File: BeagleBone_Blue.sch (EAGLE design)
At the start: 409 parts, among them J1 68000-406HLF, M1 JST_ZH_2, M2 JST_ZH_2, M3 JST_ZH_2, M4 JST_ZH_2, P10 SCHA5B0200, P2 CTIJTAG, P3 87520-0010BLF, P4 UX60SC-MB-5ST(80), Q3 MOSFET-N, Q4 MOSFET-P, U1 MPU-9250, U10 TPD4S012, U12 MT41K256M16HA, U13 MTFC4GLDEA, U15 SN74LVC2G241DCU, U16 SN74LVC1G07DCK, U3 SN74LVC1G06DCK, U4 TL5209, U5 AM3358_BZCZ_324, U6 SN74LVC1G74_DCT_8, U7 24LC_32AT-I/OT, U8 TPS2051BD, U9 TPD4S012, Y1 CM200C-32.768KAZF-UT, Y2 445C33D24M00000, Y4 ASDMB-24.576MHZ-LC-T

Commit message: Updates based on review
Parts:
- removed 108: (no value), rcl:C-EUC0402
- added C$108: 10uF 25V, SparkFun-Capacitors:CAP0805
- C108: value 10uF 25V -> (none); device SparkFun-Capacitors:CAP0805 -> rcl:C-EUC0402
- R50, R51: value (none) -> DNP
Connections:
- removed net N$242: R50.1, U5G$2.ECAP0_IN_PWM0_OUT/UART3_TXD/SPI1_CS1/PR1_ECAP0_ECAP_CAPIN_APWM_O/SPI1_SCLK/MMC0_SDWP/XDMA_EVENT_INTR2/GPIO0_7
- removed net N$244: R51.1, U5G$2.MCASP0_ACLKR/EQEP0A_IN/MCASP0_AXR2/MCASP1_ACLKX/MMC0_SDWP/PR1_PRU0_PRU_R30_4/PR1_PRU0_PRU_R31_4/GPIO3_18
- removed net SPI1_CS1: SPI1.2.6, U5G$1.GPMC_A1/GMII2_RXDV/RGMII2_RCTL/MMC2_DAT0/GPMC_A17/PR1_MII1_TXD3/EHRPWM1_SYNCI_O/GPIO1_17
- new net GPIO0_7SRC: R50.1, SPI1.2.6, U5G$2.ECAP0_IN_PWM0_OUT/UART3_TXD/SPI1_CS1/PR1_ECAP0_ECAP_CAPIN_APWM_O/SPI1_SCLK/MMC0_SDWP/XDMA_EVENT_INTR2/GPIO0_7
- new net GPIO1_17: U5G$1.GPMC_A1/GMII2_RXDV/RGMII2_RCTL/MMC2_DAT0/GPMC_A17/PR1_MII1_TXD3/EHRPWM1_SYNCI_O/GPIO1_17
- new net P9_42: R50.2, R51.2
- net GND: now also C$108.2; no longer 108.2
- net N$79: now also C$108.1; no longer C108.1
- net QEP_0A: now also R51.1, U5G$2.MCASP0_ACLKR/EQEP0A_IN/MCASP0_AXR2/MCASP1_ACLKX/MMC0_SDWP/PR1_PRU0_PRU_R30_4/PR1_PRU0_PRU_R31_4/GPIO3_18; no longer R50.2, R51.2
- net VCC: now also C108.1; no longer 108.1
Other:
- note removed: "GPIO0_7SRC"
- note removed: "GPIO3_18"
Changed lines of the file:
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@@
 <part name="R49" library="rcl" deviceset="R-US_" device="R0402"/>
 <part name="SUPPLY41" library="supply2" deviceset="GND" device="" value="DGND"/>
-<part name="R50" library="rcl" deviceset="R-US_" device="R0402"/>
-<part name="R51" library="rcl" deviceset="R-US_" device="R0402"/>
+<part name="R50" library="rcl" deviceset="R-US_" device="R0402" value="DNP"/>
+<part name="R51" library="rcl" deviceset="R-US_" device="R0402" value="DNP"/>
 <part name="U8" library="TPS2051B" deviceset="TPS2051B_D_8" device="" value="TPS2051BD"/>
 <part name="R53" library="rcl" deviceset="R-US_" device="R0402"/>
@@
 <part name="SUPPLY118" library="supply2" deviceset="GND" device="" value="DGND"/>
 <part name="C107" library="rcl" deviceset="C-EU" device="C0402"/>
-<part name="108" library="rcl" deviceset="C-EU" device="C0402"/>
+<part name="C108" library="rcl" deviceset="C-EU" device="C0402"/>
 <part name="C109" library="rcl" deviceset="C-EU" device="C0402"/>
 <part name="C110" library="rcl" deviceset="C-EU" device="C0402"/>
@@
 <part name="R39" library="Strawson_Eagle_Lib" deviceset="RESISTOR" device="0402-RES" value="4.7k"/>
 <part name="GND17" library="SparkFun-Aesthetics" deviceset="GND" device=""/>
-<part name="C108" library="SparkFun-Capacitors" deviceset="CAP" device="0805" value="10uF 25V"/>
+<part name="C$108" library="SparkFun-Capacitors" deviceset="CAP" device="0805" value="10uF 25V"/>
 <part name="C174" library="SparkFun-Capacitors" deviceset="CAP" device="0805" value="10uF 25V"/>
 <part name="C175" library="SparkFun-Capacitors" deviceset="CAP" device="0805" value="10uF 25V"/>
@@
 </segment>
 </net>
-<net name="SPI1_CS1" class="0">
+<net name="GPIO1_17" class="0">
 <segment>
 <pinref part="U5" gate="G$1" pin="GPMC_A1/GMII2_RXDV/RGMII2_RCTL/MMC2_DAT0/GPMC_A17/PR1_MII1_TXD3/EHRPWM1_SYNCI_O/GPIO1_17"/>
@@
 <text x="154.94" y="228.6" size="1.778" layer="96">USB1_DRVVBUS</text>
 <text x="157.48" y="226.06" size="1.778" layer="96">USB1_VBUS</text>
-<text x="152.4" y="210.82" size="1.778" layer="96">GPIO0_7SRC</text>
-<text x="162.56" y="200.66" size="1.778" layer="96">GPIO3_18</text>
 <text x="22.86" y="101.6" size="1.778" layer="96">USB1_DRVVBUS</text>
 <text x="111.76" y="109.22" size="1.778" layer="96">USB1_PWR</text>
@@
 </segment>
 </net>
-<net name="N$242" class="0">
+<net name="GPIO0_7SRC" class="0">
 <segment>
 <pinref part="R50" gate="G$1" pin="1"/>
 <pinref part="U5" gate="G$2" pin="ECAP0_IN_PWM0_OUT/UART3_TXD/SPI1_CS1/PR1_ECAP0_ECAP_CAPIN_APWM_O/SPI1_SCLK/MMC0_SDWP/XDMA_EVENT_INTR2/GPIO0_7"/>
 <wire x1="142.24" y1="210.82" x2="172.72" y2="210.82" width="0.1524" layer="91"/>
+<label x="152.4" y="210.82" size="1.778" layer="95"/>
 </segment>
 </net>
-<net name="QEP_0A" class="0">
+<net name="P9_42" class="0">
 <segment>
 <pinref part="R50" gate="G$1" pin="2"/>
@@
 </segment>
 </net>
-<net name="N$244" class="0">
+<net name="QEP_0A" class="0">
 <segment>
 <pinref part="R51" gate="G$1" pin="1"/>
@@
 <pinref part="U5" gate="G$2" pin="MCASP0_ACLKR/EQEP0A_IN/MCASP0_AXR2/MCASP1_ACLKX/MMC0_SDWP/PR1_PRU0_PRU_R30_4/PR1_PRU0_PRU_R31_4/GPIO3_18"/>
 <wire x1="436.88" y1="220.98" x2="419.1" y2="220.98" width="0.1524" layer="91"/>
+<label x="167.64" y="200.66" size="1.778" layer="95"/>
+<label x="436.88" y="220.98" size="1.778" layer="95"/>
 </segment>
 </net>
@@
 <instance part="SUPPLY118" gate="GND" x="182.88" y="355.6" rot="R270"/>
 <instance part="C107" gate="G$1" x="358.14" y="231.14"/>
-<instance part="108" gate="G$1" x="365.76" y="231.14"/>
+<instance part="C108" gate="G$1" x="365.76" y="231.14"/>
 <instance part="C109" gate="G$1" x="373.38" y="231.14"/>
 <instance part="C110" gate="G$1" x="381" y="231.14"/>
@@
 <wire x1="426.72" y1="215.9" x2="434.34" y2="215.9" width="0.1524" layer="91"/>
 <wire x1="434.34" y1="215.9" x2="434.34" y2="226.06" width="0.1524" layer="91"/>
-<pinref part="108" gate="G$1" pin="2"/>
+<pinref part="C108" gate="G$1" pin="2"/>
 <wire x1="365.76" y1="226.06" x2="365.76" y2="215.9" width="0.1524" layer="91"/>
 <pinref part="C109" gate="G$1" pin="2"/>
@@
 <pinref part="C109" gate="G$1" pin="1"/>
 <wire x1="373.38" y1="233.68" x2="373.38" y2="241.3" width="0.1524" layer="91"/>
-<pinref part="108" gate="G$1" pin="1"/>
+<pinref part="C108" gate="G$1" pin="1"/>
 <wire x1="365.76" y1="233.68" x2="365.76" y2="241.3" width="0.1524" layer="91"/>
 <junction x="365.76" y="241.3"/>
@@
 <instance part="R39" gate="G$1" x="102.87" y="-99.06" rot="R270"/>
 <instance part="GND17" gate="1" x="102.87" y="-107.95"/>
-<instance part="C108" gate="G$1" x="129.54" y="-11.43" smashed="yes">
+<instance part="C$108" gate="G$1" x="129.54" y="-11.43" smashed="yes">
 <attribute name="NAME" x="131.064" y="-8.509" size="1.778" layer="95"/>
 <attribute name="VALUE" x="127.889" y="-17.526" size="1.778" layer="96" rot="R90"/>
@@
 <pinref part="D11" gate="G$1" pin="C"/>
 <pinref part="D10" gate="G$1" pin="C"/>
-<pinref part="C108" gate="G$1" pin="1"/>
+<pinref part="C$108" gate="G$1" pin="1"/>
 <wire x1="132.08" y1="-1.27" x2="129.54" y2="-1.27" width="0.1524" layer="91"/>
 <wire x1="129.54" y1="-1.27" x2="129.54" y2="1.27" width="0.1524" layer="91"/>
@@
 <pinref part="D9" gate="G$1" pin="A"/>
 <wire x1="161.29" y1="-12.7" x2="161.29" y2="-19.05" width="0.1524" layer="91"/>
-<pinref part="C108" gate="G$1" pin="2"/>
+<pinref part="C$108" gate="G$1" pin="2"/>
 <pinref part="C174" gate="G$1" pin="2"/>
 <wire x1="182.88" y1="-12.7" x2="182.88" y2="-19.05" width="0.1524" layer="91"/>
@@
 </segment>
 </net>
-<net name="SPI1_CS1" class="0">
-<segment>
-<wire x1="236.22" y1="-114.3" x2="222.25" y2="-114.3" width="0.1524" layer="91"/>
-<label x="223.52" y="-114.3" size="1.778" layer="95"/>
-<pinref part="SPI1.2" gate="G$1" pin="6"/>
-</segment>
-</net>
 <net name="IMU_INT" class="0">
 <segment>
@@
 </segment>
 </net>
-<net name="QEP_0A" class="0">
-<segment>
-<wire x1="231.14" y1="-54.61" x2="218.44" y2="-54.61" width="0.1524" layer="91"/>
-<label x="232.41" y="-54.61" size="1.778" layer="95" rot="MR0"/>
-<pinref part="R168" gate="G$1" pin="1"/>
-<wire x1="218.44" y1="-50.8" x2="218.44" y2="-54.61" width="0.1524" layer="91"/>
-<pinref part="E1" gate="G$1" pin="3"/>
-</segment>
-</net>
 <net name="UART2_TX" class="0">
 <segment>
@@
 </segment>
 </net>
+<net name="GPIO0_7SRC" class="0">
+<segment>
+<pinref part="SPI1.2" gate="G$1" pin="6"/>
+<wire x1="236.22" y1="-114.3" x2="223.52" y2="-114.3" width="0.1524" layer="91"/>
+<label x="223.52" y="-114.3" size="1.778" layer="95"/>
+</segment>
+</net>
+<net name="QEP_0A" class="0">
+<segment>
+<pinref part="R168" gate="G$1" pin="1"/>
+<wire x1="218.44" y1="-50.8" x2="220.98" y2="-50.8" width="0.1524" layer="91"/>
+<wire x1="220.98" y1="-50.8" x2="220.98" y2="-54.61" width="0.1524" layer="91"/>
+<wire x1="220.98" y1="-54.61" x2="231.14" y2="-54.61" width="0.1524" layer="91"/>
+<wire x1="231.394" y1="-54.61" x2="231.14" y2="-54.61" width="0.1524" layer="91"/>
+<pinref part="E1" gate="G$1" pin="3"/>
+<label x="223.012" y="-54.102" size="1.778" layer="95"/>
+</segment>
+</net>

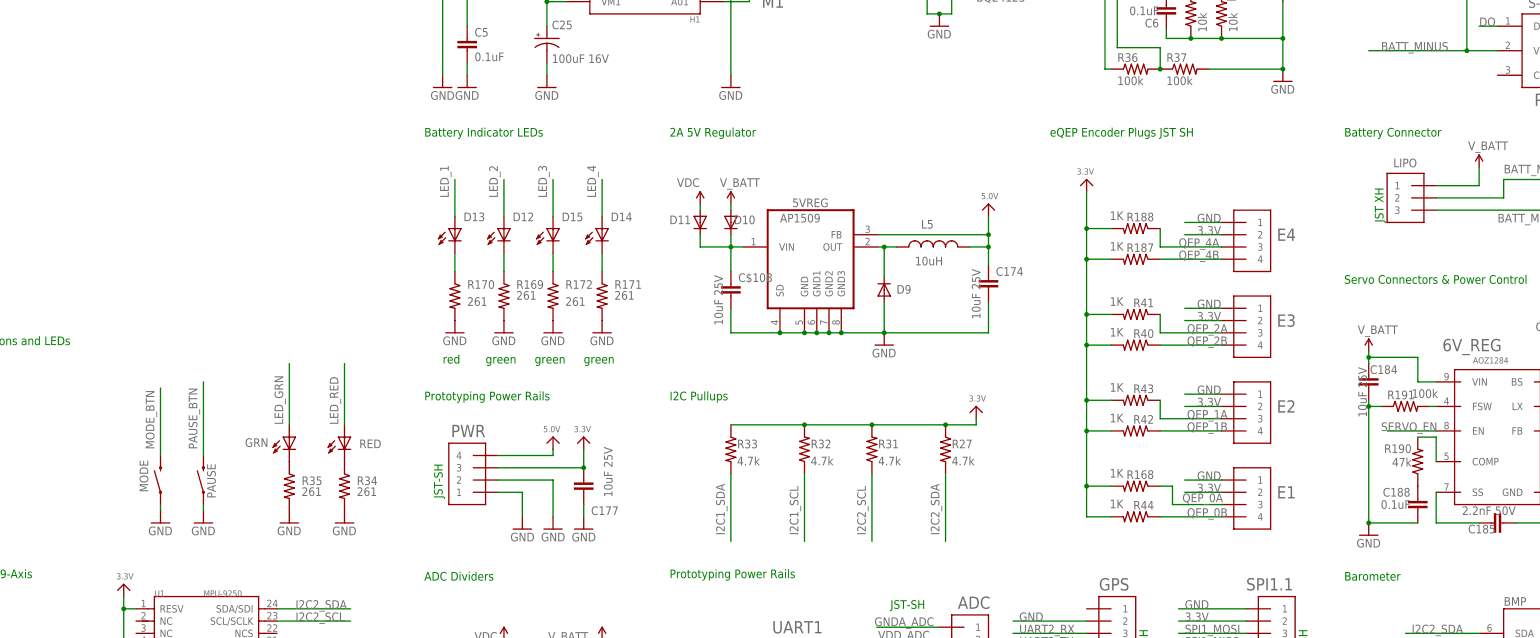
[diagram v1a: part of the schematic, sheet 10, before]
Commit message: add pulldowns on servo channels
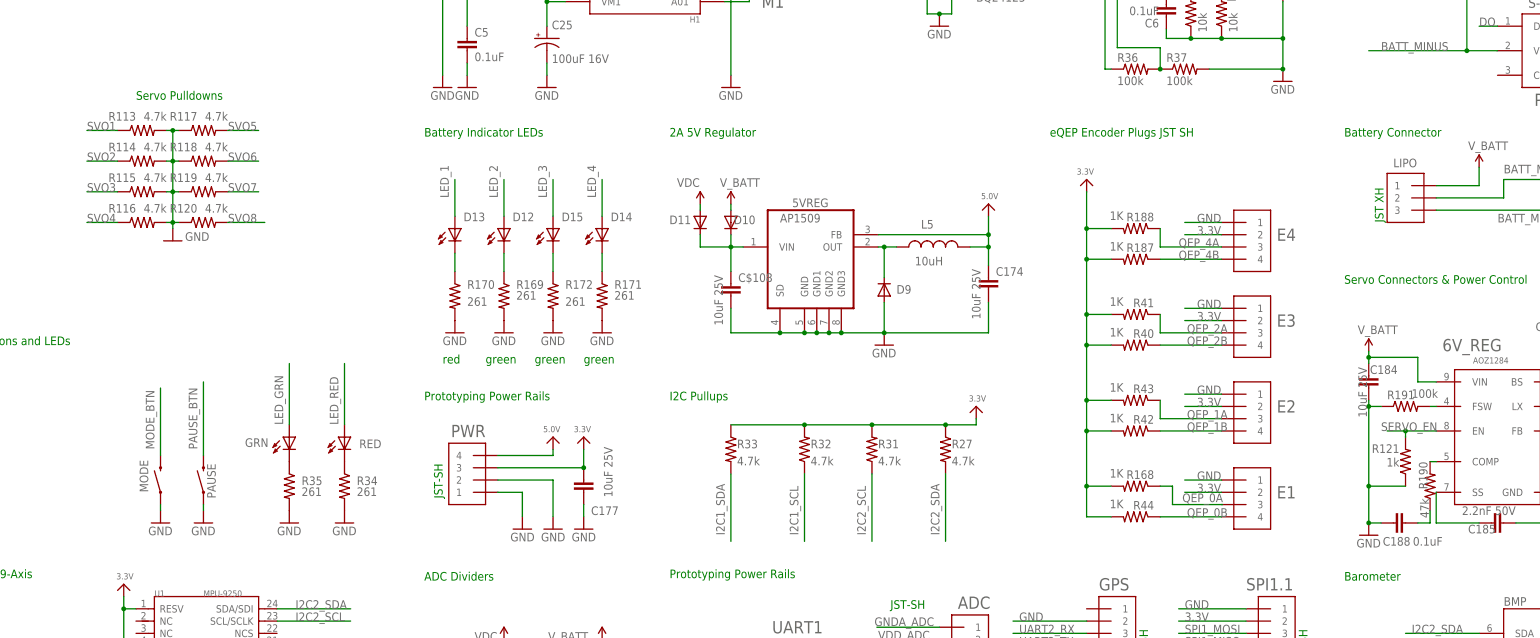
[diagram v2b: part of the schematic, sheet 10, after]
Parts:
- added R113, R114, R115, R116, R117, R118, R119, R120: 4.7k, Strawson_Eagle_Lib:RESISTOR0402-RES
- added R121: 1k, Strawson_Eagle_Lib:RESISTOR0402-RES
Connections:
- net GND: now also R113.2, R114.2, R115.2, R116.2, R117.1, R118.1, R119.1, R120.1, R121.1
- net SERVO_EN: now also R121.2
- net SVO1: now also R113.1
- net SVO2: now also R114.1
- net SVO3: now also R115.1
- net SVO4: now also R116.1
- net SVO5: now also R117.2
- net SVO6: now also R118.2
- net SVO7: now also R119.2
- net SVO8: now also R120.2
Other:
- note added: "Servo Pulldowns"
- moved on the sheet: C188, R190

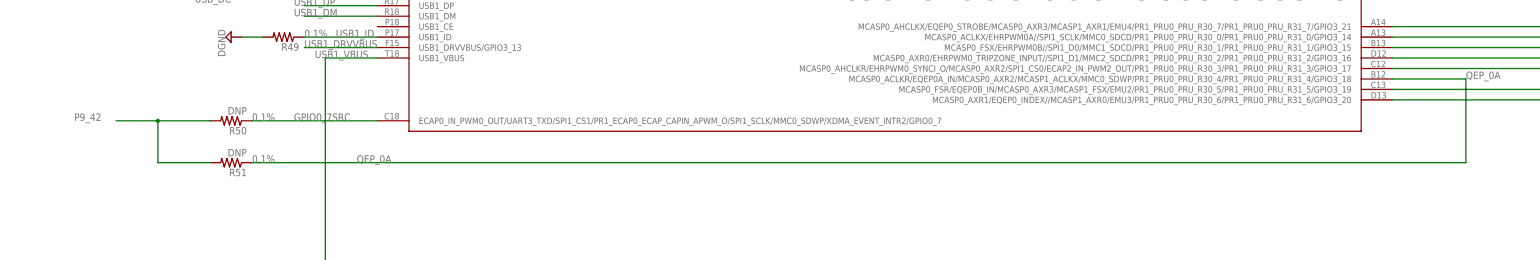
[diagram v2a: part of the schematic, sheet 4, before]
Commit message: split C18 & B12 which were connected on the cape
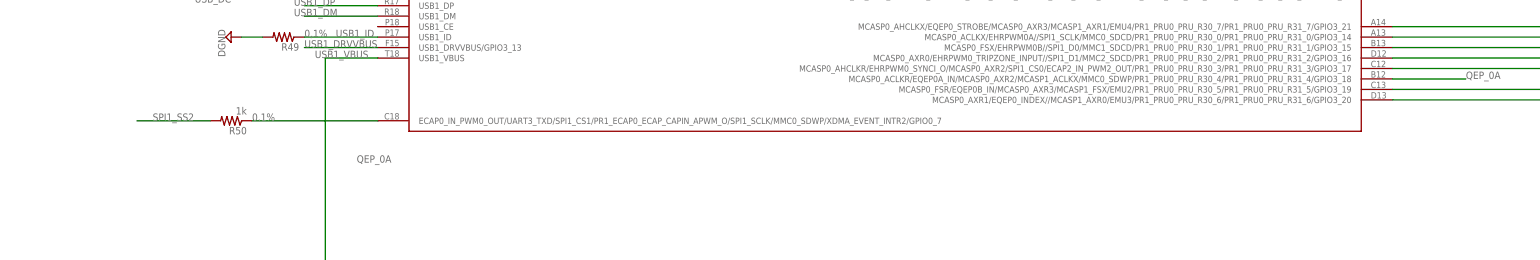
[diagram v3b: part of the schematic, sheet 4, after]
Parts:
- removed R51: DNP, rcl:R-US_R0402
- R50: value DNP -> 1k
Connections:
- removed net P9_42: R50.2, R51.2
- new net SPI1_SS2: R50.2
- net QEP_0A: no longer R51.1
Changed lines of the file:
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@@
 <part name="R49" library="rcl" deviceset="R-US_" device="R0402"/>
 <part name="SUPPLY41" library="supply2" deviceset="GND" device="" value="DGND"/>
-<part name="R50" library="rcl" deviceset="R-US_" device="R0402" value="DNP"/>
-<part name="R51" library="rcl" deviceset="R-US_" device="R0402" value="DNP"/>
+<part name="R50" library="rcl" deviceset="R-US_" device="R0402" value="1k"/>
 <part name="U8" library="TPS2051B" deviceset="TPS2051B_D_8" device="" value="TPS2051BD"/>
 <part name="R53" library="rcl" deviceset="R-US_" device="R0402"/>
@@
 <text x="154.94" y="231.14" size="1.778" layer="96">0,1%</text>
 <text x="142.24" y="210.82" size="1.778" layer="96">0,1%</text>
-<text x="142.24" y="200.66" size="1.778" layer="96">0,1%</text>
 <text x="139.7" y="119.38" size="1.778" layer="96" rot="R90">10K,1%</text>
 <text x="30.48" y="83.82" size="1.778" layer="96" rot="R90">10K,1%</text>
@@
 <instance part="SUPPLY41" gate="GND" x="137.16" y="231.14" rot="R270"/>
 <instance part="R50" gate="G$1" x="137.16" y="210.82" rot="R180"/>
-<instance part="R51" gate="G$1" x="137.16" y="200.66" rot="R180"/>
 <instance part="U8" gate="A" x="53.34" y="109.22"/>
 <instance part="R53" gate="G$1" x="33.02" y="86.36" rot="R270"/>
@@
 <pinref part="U5" gate="G$2" pin="ECAP0_IN_PWM0_OUT/UART3_TXD/SPI1_CS1/PR1_ECAP0_ECAP_CAPIN_APWM_O/SPI1_SCLK/MMC0_SDWP/XDMA_EVENT_INTR2/GPIO0_7"/>
 <wire x1="142.24" y1="210.82" x2="172.72" y2="210.82" width="0.1524" layer="91"/>
-<label x="152.4" y="210.82" size="1.778" layer="95"/>
-</segment>
-</net>
-<net name="P9_42" class="0">
-<segment>
-<pinref part="R50" gate="G$1" pin="2"/>
-<wire x1="132.08" y1="210.82" x2="119.38" y2="210.82" width="0.1524" layer="91"/>
-<wire x1="119.38" y1="210.82" x2="119.38" y2="200.66" width="0.1524" layer="91"/>
-<pinref part="R51" gate="G$1" pin="2"/>
-<wire x1="132.08" y1="200.66" x2="119.38" y2="200.66" width="0.1524" layer="91"/>
-<wire x1="119.38" y1="210.82" x2="109.22" y2="210.82" width="0.1524" layer="91"/>
-<junction x="119.38" y="210.82"/>
-<label x="99.06" y="210.82" size="1.778" layer="95"/>
 </segment>
 </net>
 <net name="QEP_0A" class="0">
 <segment>
-<pinref part="R51" gate="G$1" pin="1"/>
-<wire x1="142.24" y1="200.66" x2="436.88" y2="200.66" width="0.1524" layer="91"/>
-<wire x1="436.88" y1="200.66" x2="436.88" y2="220.98" width="0.1524" layer="91"/>
 <pinref part="U5" gate="G$2" pin="MCASP0_ACLKR/EQEP0A_IN/MCASP0_AXR2/MCASP1_ACLKX/MMC0_SDWP/PR1_PRU0_PRU_R30_4/PR1_PRU0_PRU_R31_4/GPIO3_18"/>
 <wire x1="436.88" y1="220.98" x2="419.1" y2="220.98" width="0.1524" layer="91"/>
@@
 </segment>
 </net>
+<net name="SPI1_SS2" class="0">
+<segment>
+<pinref part="R50" gate="G$1" pin="2"/>
+<wire x1="132.08" y1="210.82" x2="114.3" y2="210.82" width="0.1524" layer="91"/>
+<label x="118.11" y="210.82" size="1.778" layer="95"/>
+</segment>
+</net>
